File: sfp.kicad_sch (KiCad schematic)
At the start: 33 parts, among them J12 Bel-Fuse_SFP+_1x20_SS-79100-0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

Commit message: [#83396] Route SFI
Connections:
- net SFI_CONN_TX_N: now also J12.18 (TD+); no longer J12.19 (TD-)
- net SFI_CONN_TX_P: now also J12.19 (TD-); no longer J12.18 (TD+)
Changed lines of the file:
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@@
 	(wire
 		(pts
+			(xy 182.88 151.13) (xy 185.42 151.13)
+		)
+		(stroke
+			(width 0)
+			(type default)
+		)
+	)
+	(wire
+		(pts
 			(xy 166.37 115.57) (xy 166.37 113.03)
 		)
@@
 	(wire
 		(pts
+			(xy 182.88 153.67) (xy 185.42 153.67)
+		)
+		(stroke
+			(width 0)
+			(type default)
+		)
+	)
+	(wire
+		(pts
 			(xy 287.02 156.21) (xy 287.02 161.29)
 		)
@@
 	(wire
 		(pts
-			(xy 156.21 151.13) (xy 185.42 151.13)
+			(xy 156.21 151.13) (xy 180.34 151.13)
 		)
 		(stroke
@@
 	(wire
 		(pts
+			(xy 180.34 153.67) (xy 182.88 151.13)
+		)
+		(stroke
+			(width 0)
+			(type default)
+		)
+	)
+	(wire
+		(pts
 			(xy 246.38 127) (xy 246.38 128.27)
 		)
@@
 	(wire
 		(pts
-			(xy 160.02 153.67) (xy 185.42 153.67)
+			(xy 160.02 153.67) (xy 180.34 153.67)
 		)
 		(stroke
@@
 	(wire
 		(pts
+			(xy 180.34 151.13) (xy 182.88 153.67)
+		)
+		(stroke
+			(width 0)
+			(type default)
+		)
+	)
+	(wire
+		(pts
 			(xy 166.37 135.89) (xy 185.42 135.89)
 		)
@@
 	)
 	(label "SFI_CONN_TX_P"
-		(at 168.91 151.13 0)
+		(at 165.1 151.13 0)
 		(effects
 			(font
@@
 	)
 	(label "SFI_CONN_RX_P"
-		(at 168.91 158.75 0)
+		(at 165.1 158.75 0)
 		(effects
 			(font
@@
 	)
 	(label "SFI_CONN_TX_N"
-		(at 168.91 153.67 0)
+		(at 165.1 153.67 0)
 		(effects
 			(font
@@
 	)
 	(label "SFI_CONN_RX_N"
-		(at 168.91 161.29 0)
+		(at 165.1 161.29 0)
 		(effects
 			(font

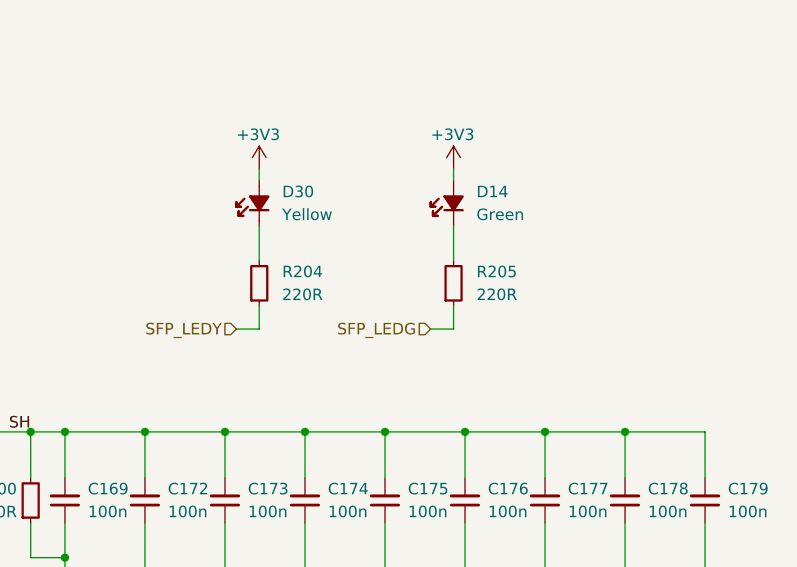
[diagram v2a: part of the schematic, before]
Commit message: [#83396] Implement small post review fixes eg. correct LED resistor values, update sheet table, delete four wire connections
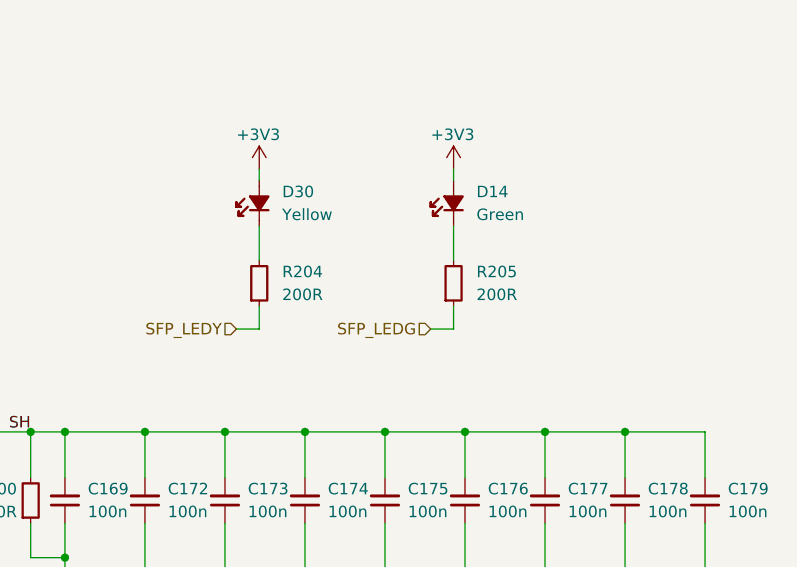
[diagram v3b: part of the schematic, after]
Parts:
- removed R204, R205: R_220R_0402, antmicro-footprints:R_0402_1005Metric, symbol antmicroResistors0402:R_220R_0402
- added R204, R205: R_200R_0402, antmicro-footprints:R_0402_1005Metric, symbol antmicroResistors0402:R_200R_0402
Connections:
- net SFP_LEDG: now also R205.1
- net SFP_LEDY: now also R204.1
- net at D30.1 (C): now also R204.2
- net at D14.1 (C): now also R205.2

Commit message: [#85326] Add reviewers suggestions; Unify BOM
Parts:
- C168: value C_22u_10V_0603 -> C_22u_16V_0603; footprint antmicro-footprints:C_0603_1608Metric -> antmicro-footprints:C_0603_1608Metric_EIA; symbol antmicroCapacitors0603:C_22u_10V_0603 -> antmicroCapacitors0603:C_22u_16V_0603; MPN GRM188R61A226ME15D -> CL10A226MO7JZNC; Manufacturer Murata -> Samsung Electro-Mechanics; Voltage 10V -> 16V
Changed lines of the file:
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@@
 	)
 	(symbol
-		(lib_id "antmicroCapacitors0603:C_22u_10V_0603")
+		(lib_id "antmicroCapacitors0603:C_22u_16V_0603")
 		(at 156.21 99.06 90)
 		(unit 1)
@@
 			)
 		)
-		(property "Value" "C_22u_10V_0603"
+		(property "Value" "C_22u_16V_0603"
 			(at 166.37 78.74 0)
 			(effects
@@
 			)
 		)
-		(property "Footprint" "antmicro-footprints:C_0603_1608Metric"
+		(property "Footprint" "antmicro-footprints:C_0603_1608Metric_EIA"
 			(at 168.91 78.74 0)
 			(effects
@@
 			)
 		)
-		(property "Datasheet" "https://www.murata.com/products/productdetail?partno=GRM188R61A226ME15%23"
+		(property "Datasheet" "https://product.samsungsem.com/mlcc/CL10A226MO7JZN.do"
 			(at 171.45 78.74 0)
 			(effects
@@
 			)
 		)
-		(property "Description" "22 µF ±20% 10V Ceramic Capacitor X5R 0603 (1608 Metric)"
+		(property "Description" "SMD Multilayer Ceramic Capacitor"
 			(at 156.21 99.06 0)
 			(effects
@@
 			)
 		)
-		(property "MPN" "GRM188R61A226ME15D"
+		(property "MPN" "CL10A226MO7JZNC"
 			(at 173.99 78.74 0)
 			(effects
@@
 			)
 		)
-		(property "Manufacturer" "Murata"
+		(property "Manufacturer" "Samsung Electro-Mechanics"
 			(at 176.53 78.74 0)
 			(effects
@@
 			)
 		)
-		(property "Voltage" "10V"
+		(property "Voltage" "16V"
 			(at 184.15 78.74 0)
 			(effects
